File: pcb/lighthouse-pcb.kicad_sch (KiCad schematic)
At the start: 54 parts, among them J1 USB_C_Receptacle_USB2.0, SW1 BOOT/ROOF, SW2 RESET, SW3 FRONT, SW4 SW_DIP_x08, U1 ESP32-C3-WROOM-02, U2 CN5711, U3 AP2112K-3.3, U4 USBLC6-2SC6

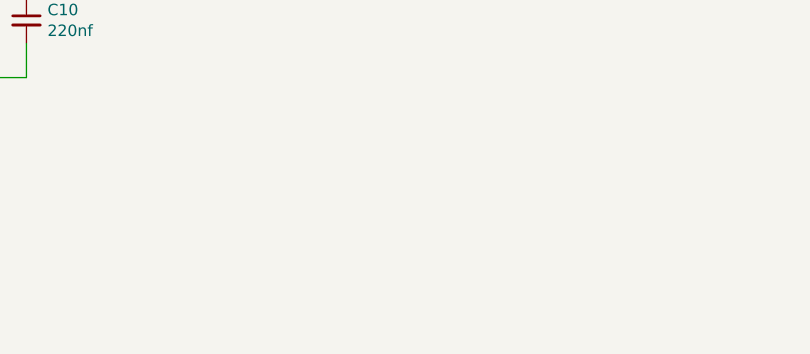
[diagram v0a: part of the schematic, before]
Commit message: Add information for panelization
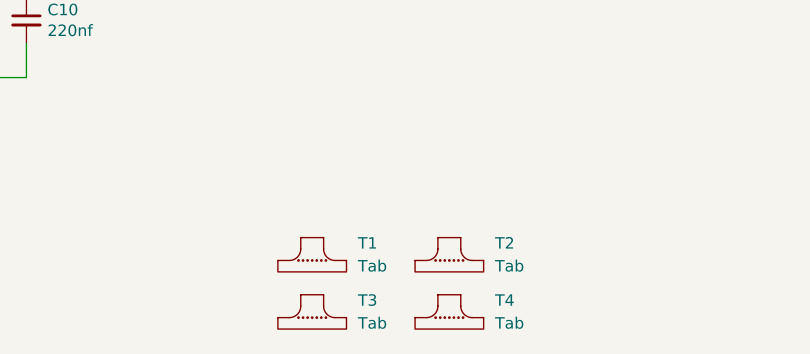
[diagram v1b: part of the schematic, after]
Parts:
- added T1, T2, T3, T4: Tab, PCM_kikit:Tab, symbol PCM_kikit:Tab
